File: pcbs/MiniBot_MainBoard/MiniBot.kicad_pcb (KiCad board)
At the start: 4 copper layers, 21.2 x 28 mm, 60 parts, among them IC1 MMC5633NJL, IC2 MIC23050-SYML-TR, J1 Conn_01x08, J2 Conn_01x02, J3 GSB1C41110SSHR, J4 Conn_01x01, U1 ESP32-C3-MINI-1-H4X, U3 MCP73832-2-OT, U4 STSPIN220, U5 STSPIN220

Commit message: led updates
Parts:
- removed D1, D2: LED, Diode_SMD:D_0402_1005Metric
- removed J4: Conn_01x01, TestPoint:TestPoint_Pad_D1.0mm
- removed R17: 5.1k, Resistor_SMD:R_0402_1005Metric
- added LED1: EASV2010RWA0, SamacSys_Parts:EASV2010RWA0, B.Cu at (121.3, 85.4)
- added R4: 10k, Resistor_SMD:R_0402_1005Metric, B.Cu at (127.2, 90.4)
- R8: value 15k -> 12.4k
- moved JP1 1.63 mm to (121.6, 87.9)
- moved IC1 0.66 mm to (128.6, 107.6)
- moved R13 0.61 mm to (124.9, 88.1), turned to 90 degrees
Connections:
- R13 pad 1: Net-(D2-K) -> /LED_R
- U1 pad 12: /GPIO0 -> /LED_W
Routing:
- net +3V3: track 37.1 -> 57.3 mm, vias 12 -> 13
- net /LED_W: track 0.00 -> 20.1 mm, vias 0 -> 2
- net Net-(LED1-T1-): track 0.00 -> 9.23 mm
- net /GPIO0: track 7.22 -> 0.00 mm, vias 2 -> 0
- net /LED_R: track 0.00 -> 6.80 mm
- net GND: track 94.3 -> 97.6 mm, vias 24 -> 23
- net Net-(D2-K): track 2.47 -> 0.00 mm, vias 1 -> 0
- net Net-(D1-A): track 0.99 -> 0.00 mm
- net /MODE2: track 29.2 -> 28.4 mm
- net +BATT: track 25.8 -> 26.2 mm, vias 0 -> 1
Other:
- board text removed: "3v3"
- board text removed: "CHG"
- board text removed: "M1"
- board text removed: "M2"

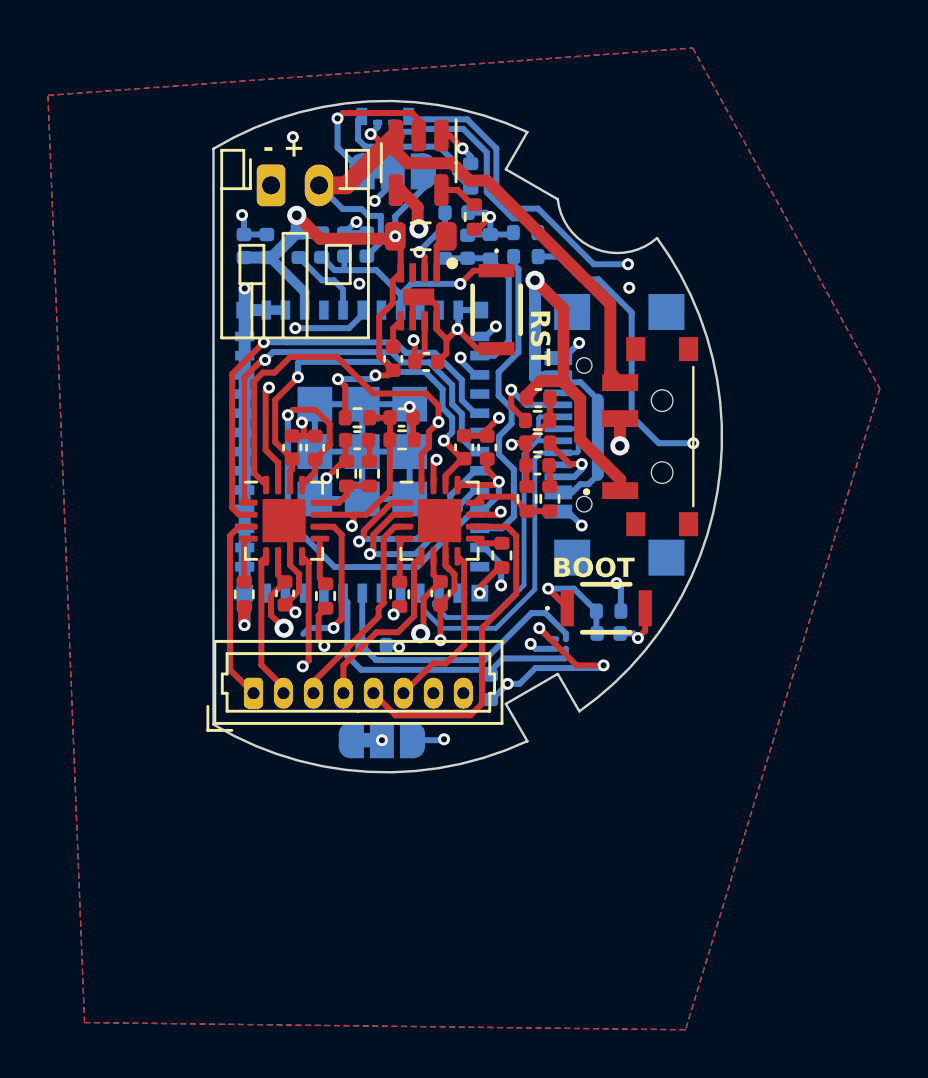
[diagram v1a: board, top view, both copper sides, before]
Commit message: improved pcb thermals
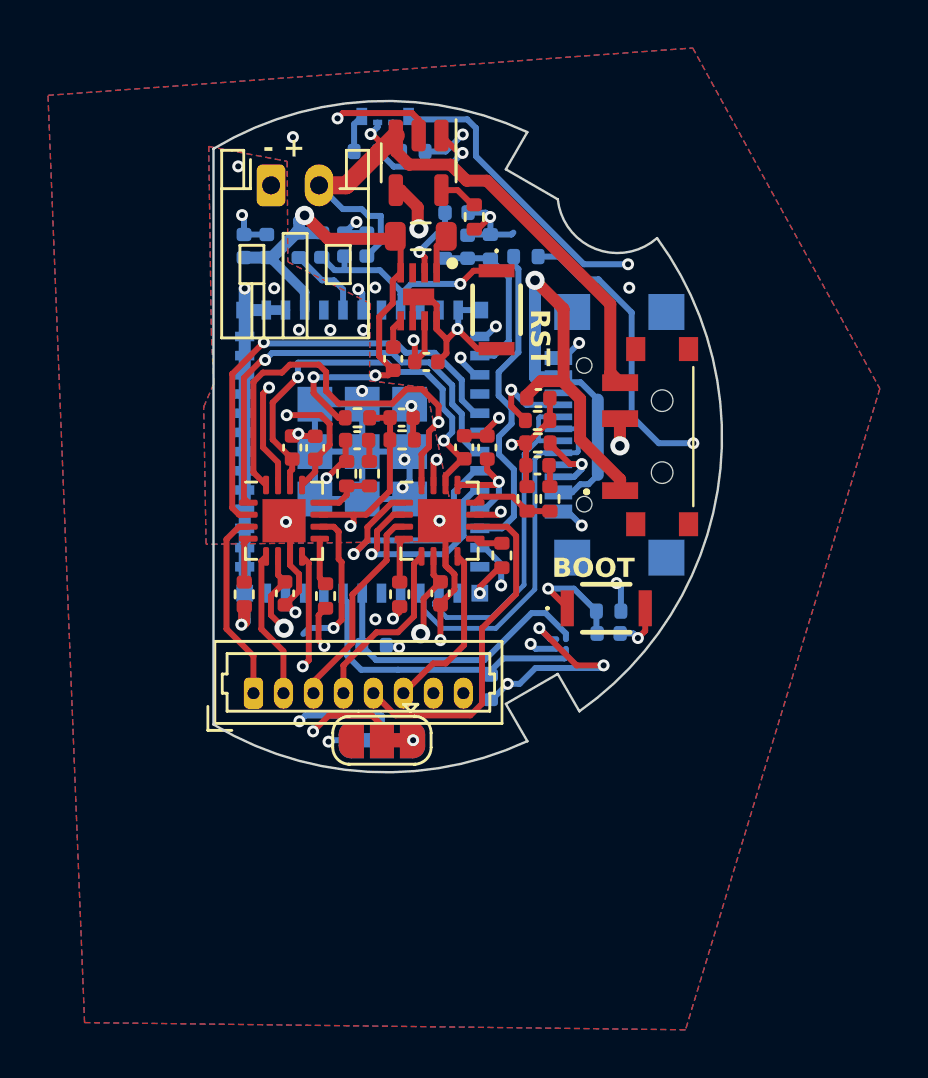
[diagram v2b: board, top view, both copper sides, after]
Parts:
- JP1: moved to F.Cu
- moved JP1 23.7 mm to (121.2, 111.6), turned to 180 degrees
- moved R4 5.79 mm to (122.5, 87.0), turned to 0 degrees
- moved R13 4.47 mm to (120.5, 87.0), turned to 0 degrees
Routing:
- net /MODE2: track 28.4 -> 38.9 mm
- net Net-(LED1-T1-): track 9.23 -> 1.35 mm
- net /LED_R: track 6.80 -> 1.59 mm
- net /MODE1: track 41.9 -> 46.5 mm
- net /M_EN: track 23.8 -> 20.0 mm
- net Net-(U3-STAT): track 1.88 -> 5.18 mm
- net /M_RST: track 22.7 -> 24.9 mm
- net /M1_DIR: track 9.18 -> 11.0 mm
- net GND: track 97.6 -> 96.0 mm, vias 23 -> 34
- net +3V3: track 57.3 -> 56.6 mm, vias 13 -> 14
- net /M1_STEP: track 8.27 -> 8.91 mm
- added copper zone on B.Cu, net GND
- added copper zone on F.Cu, net GND

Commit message: cleanup minibot schematic
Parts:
- moved R13 0.18 mm to (120.5, 87.2)
- moved R4 0.18 mm to (122.4, 87.2)
- moved LED1 0.16 mm to (121.3, 85.5)
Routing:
- net /M0_B1: track 13.0 -> 11.6 mm
- net GND: track 96.0 -> 94.9 mm, vias 34 -> 33
- net /M_RST: track 24.9 -> 25.7 mm
- net /M0_DIR: track 18.3 -> 18.9 mm
- net /M0_STEP: track 19.0 -> 19.5 mm
- net Net-(U3-STAT): track 5.18 -> 5.69 mm
- net +3V3: vias 14 -> 13
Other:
- board text added: "M1"
- board text added: "M2"

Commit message: checkpoint
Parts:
- moved R1 0.98 mm to (126.2, 108.5)
- moved R5 0.65 mm to (126.7, 91.0), turned to -90 degrees
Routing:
- net +3V3: track 56.6 -> 57.6 mm
- net /MODE1: track 46.5 -> 45.5 mm
- net /M_RST: track 25.7 -> 25.2 mm

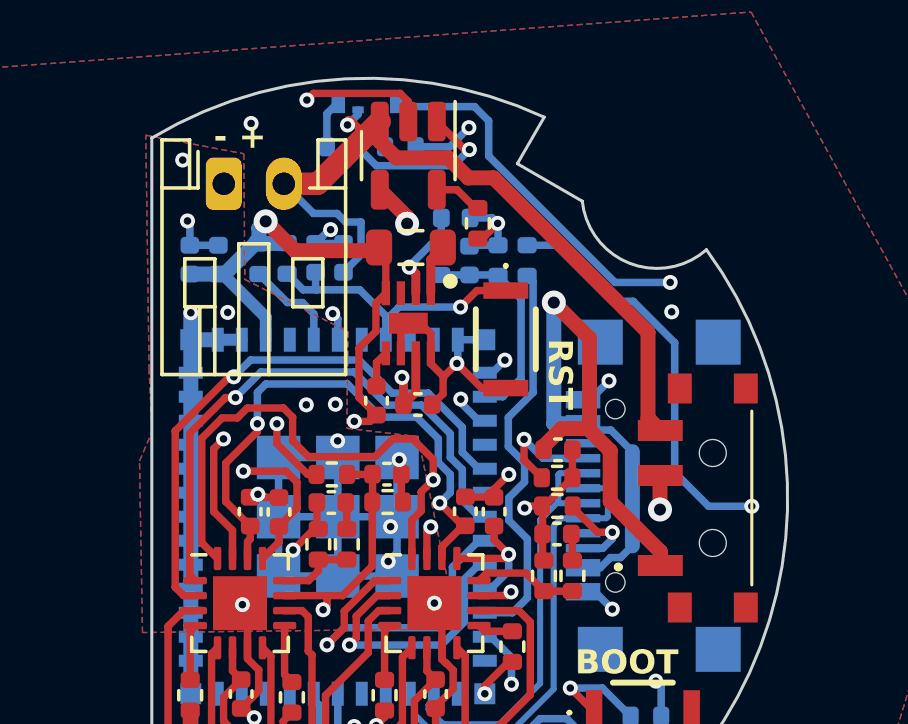
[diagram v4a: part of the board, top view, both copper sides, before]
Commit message: moving imported parts from my global dir to within this repo
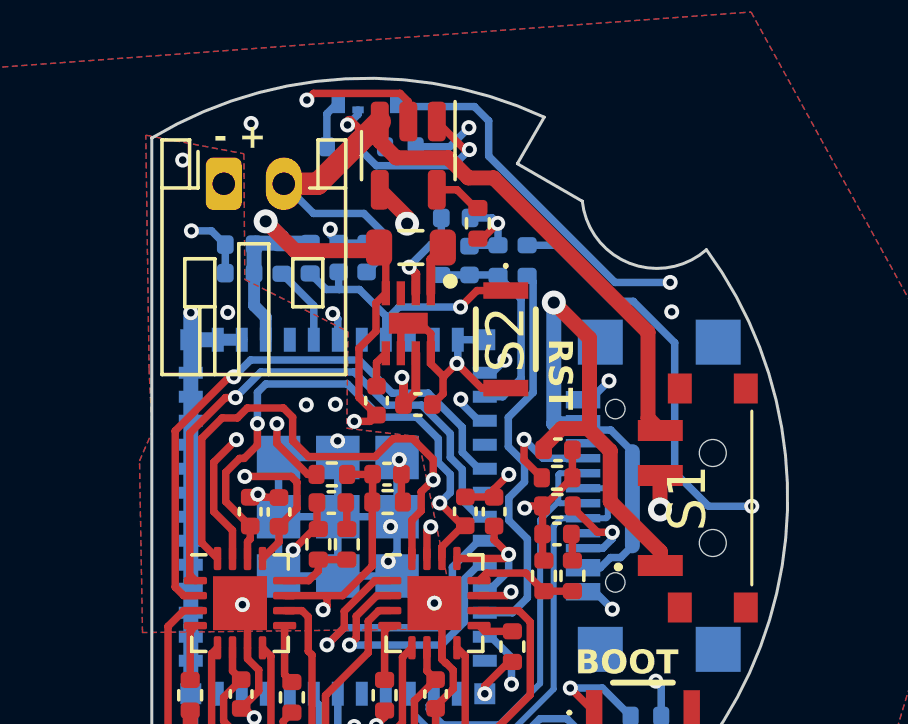
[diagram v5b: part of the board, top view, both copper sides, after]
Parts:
- IC1: footprint SamacSys_Parts:BGA4C40P2X2_85X85X60 -> minibot:BGA4C40P2X2_85X85X60
- J3: footprint SamacSys_Parts:GSB1C41110SSHR -> minibot:GSB1C41110SSHR
- LED1: footprint SamacSys_Parts:EASV2010RWA0 -> minibot:EASV2010RWA0
- S1: footprint SamacSys_Parts:PCM12SMTR -> minibot:PCM12SMTR
- S2, S3: footprint SamacSys_Parts:EVPAWBD4A -> minibot:EVPAWBD4A
- U1: footprint SamacSys_Parts:ESP32C3MINI1H4X -> minibot:ESP32C3MINI1H4X
- moved C2 1.72 mm to (117.1, 91.4), turned to 180 degrees
- moved C1 0.87 mm to (117.1, 90.5), turned to 0 degrees
- moved R3 0.77 mm to (119.4, 90.9)
- moved C10 0.77 mm to (121.3, 90.9)
- moved C3 0.77 mm to (120.4, 90.9)
- moved R6 0.77 mm to (118.5, 90.9)
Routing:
- net +3V3: track 57.6 -> 56.3 mm
- net /RST: track 9.67 -> 8.90 mm
- net /GPIO2: track 3.24 -> 2.64 mm
- net +BATT: track 26.2 -> 26.8 mm

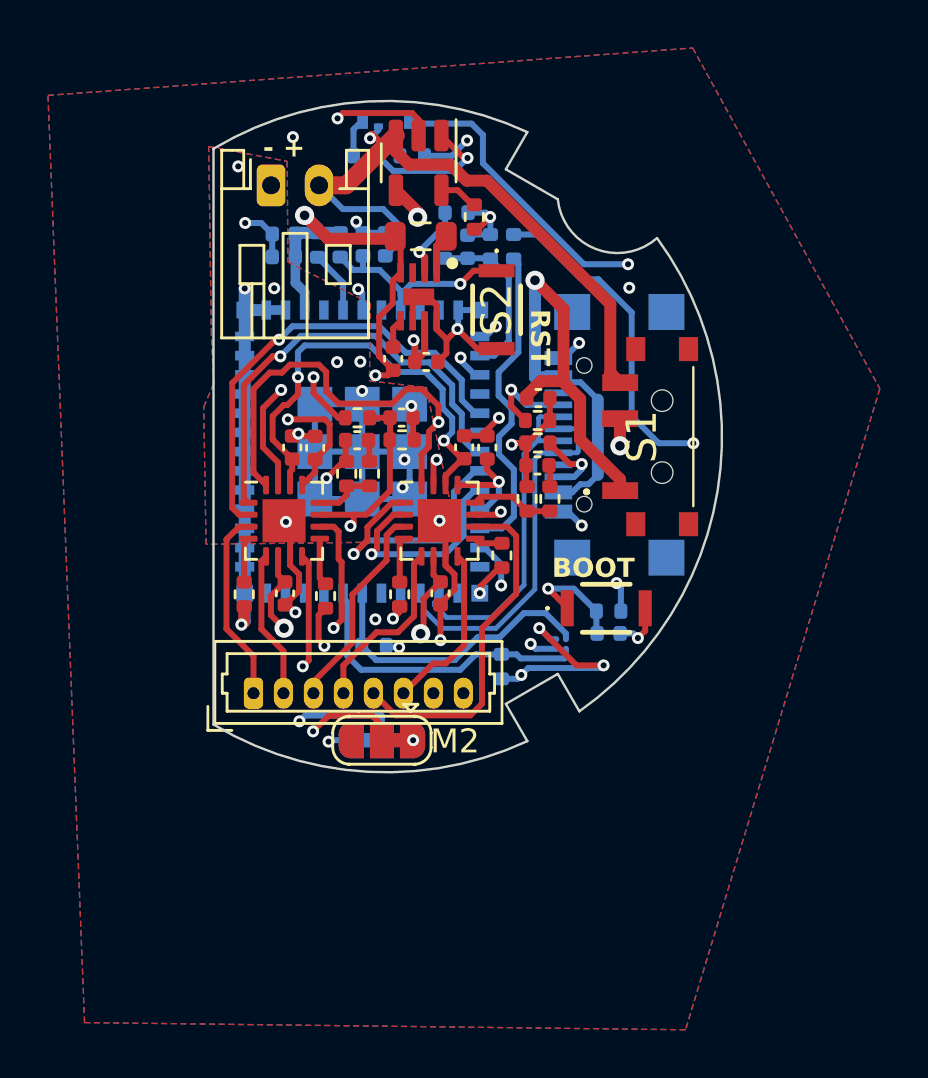
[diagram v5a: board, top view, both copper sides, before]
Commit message: mostly finished server pcb, added pogo charge pins to bots, started charge case pcb
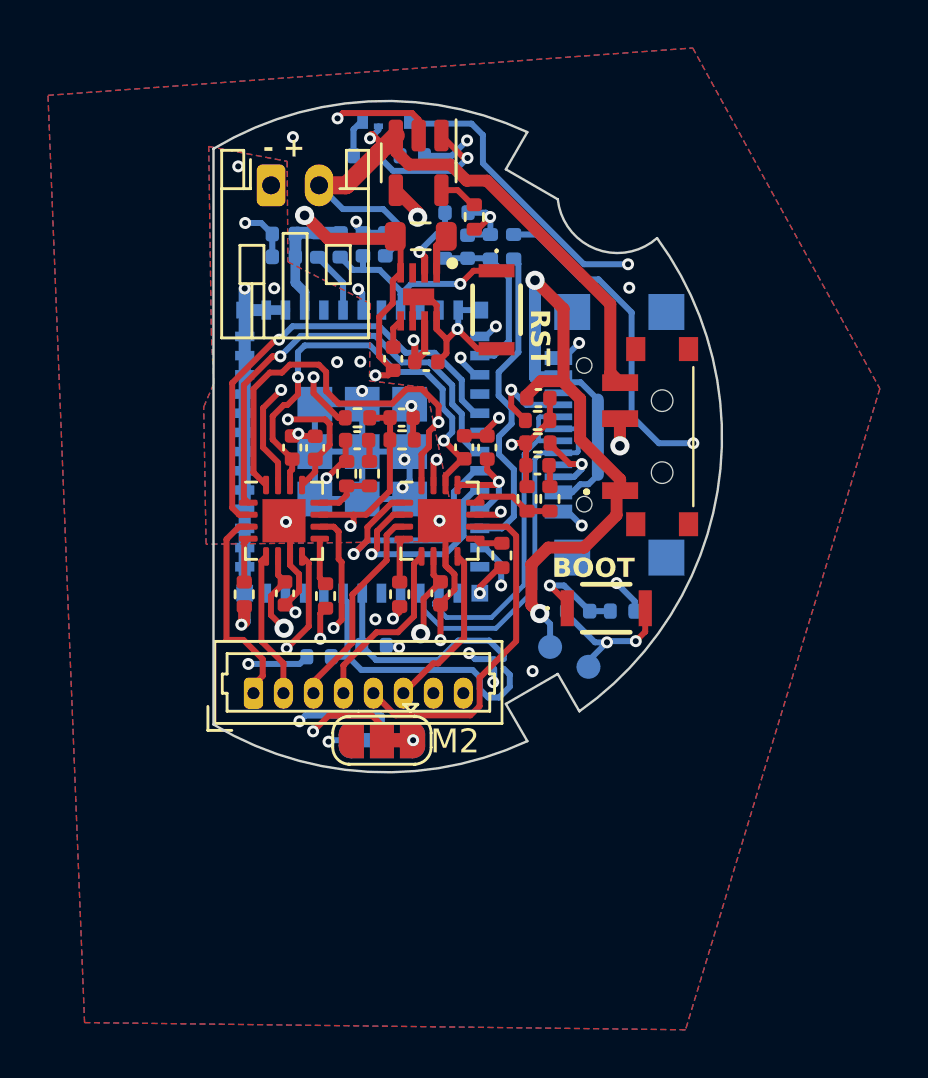
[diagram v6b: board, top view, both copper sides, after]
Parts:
- added TP1: TestPoint, TestPoint:TestPoint_Pad_D1.0mm, B.Cu at (129.8, 108.5)
- added TP2: TestPoint, TestPoint:TestPoint_Pad_D1.0mm, B.Cu at (128.2, 107.7)
- moved R1 7.61 mm to (118.5, 108.1), turned to 0 degrees
- moved IC1 2.72 mm to (126.0, 108.4)
- moved C5 1.57 mm to (129.3, 106.2), turned to 180 degrees
- moved R9 0.58 mm to (131.2, 106.2)
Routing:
- net +5V: track 31.8 -> 41.0 mm, vias 2 -> 3
- net GND: track 95.4 -> 98.6 mm, vias 33 -> 34
- net /SDA: track 12.1 -> 8.91 mm
- net +3V3: track 56.3 -> 54.0 mm
- net /M0_A1: track 8.01 -> 8.75 mm
- net /SCL: track 12.5 -> 12.0 mm
- net /M0_B2: track 10.7 -> 11.2 mm

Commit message: gitignore and pcb updates
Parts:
- moved JP1 0.12 mm to (121.2, 111.7)
- moved JP2 0.12 mm to (121.2, 111.7)
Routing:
- net +3V3: track 54.0 -> 54.9 mm
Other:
- board text added: "+"
- board text added: "-"
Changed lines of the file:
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@@
   )
   (footprint "Jumper:SolderJumper-3_P1.3mm_Bridged12_RoundedPad1.0x1.5mm" (layer "F.Cu")
-    (at 121.17 111.58 180)
+    (at 121.17 111.7 180)
     (descr "SMD Solder 3-pad Jumper, 1x1.5mm rounded Pads, 0.3mm gap, pads 1-2 bridged with 1 copper strip")
     (tags "net tie solder jumper bridged")
@@
   )
   (footprint "Jumper:SolderJumper-3_P1.3mm_Bridged12_RoundedPad1.0x1.5mm" (layer "B.Cu")
-    (at 121.17 111.58)
+    (at 121.17 111.7)
     (descr "SMD Solder 3-pad Jumper, 1x1.5mm rounded Pads, 0.3mm gap, pads 1-2 bridged with 1 copper strip")
     (tags "net tie solder jumper bridged")
@@
   (gr_line (start 121.345 98.94) (end 121.345 112.940014)
     (stroke (width 0.1) (type default)) (layer "F.Fab"))
+  (gr_text "+" (at 127.65 107.75) (layer "B.SilkS")
+    (effects (font (size 0.8 0.8) (thickness 0.15) bold) (justify left bottom mirror))
+  )
+  (gr_text "-" (at 131.55 108.8) (layer "B.SilkS")
+    (effects (font (size 0.8 0.8) (thickness 0.15) bold) (justify left bottom mirror))
+  )
   (gr_text "M1" (at 125.44 112.17) (layer "B.SilkS")
     (effects (font (size 1 1) (thickness 0.15)) (justify left bottom mirror))
@@
   (via (at 124.32 94.44) (size 0.5) (drill 0.25) (layers "F.Cu" "B.Cu") (net 15))
   (via (at 115.45 92.75) (size 0.5) (drill 0.25) (layers "F.Cu" "B.Cu") (net 15))
-  (via (at 122.47 111.58) (size 0.5) (drill 0.25) (layers "F.Cu" "B.Cu") (net 15))
+  (via (at 122.47 111.700002) (size 0.5) (drill 0.25) (layers "F.Cu" "B.Cu") (net 15))
   (via (at 131.749988 107.45) (size 0.5) (drill 0.25) (layers "F.Cu" "B.Cu") (net 15))
   (via (at 118.6 107.35002) (size 0.5) (drill 0.25) (layers "F.Cu" "B.Cu") (net 15))
@@
   (segment (start 121.95 92.1) (end 121.95 90.8) (width 0.25) (layer "F.Cu") (net 19))
   (segment (start 121.62 92.43) (end 121.95 92.1) (width 0.25) (layer "F.Cu") (net 19))
+  (segment (start 119.809319 111.639319) (end 119.87 111.7) (width 0.25) (layer "F.Cu") (net 19))
   (segment (start 121.43 96.37) (end 121.64 96.16) (width 0.25) (layer "F.Cu") (net 19))
   (segment (start 121.055 95.575) (end 121.055 93.935) (width 0.25) (layer "F.Cu") (net 19))
@@
   (segment (start 121.62 93.37) (end 121.62 92.43) (width 0.25) (layer "F.Cu") (net 19))
   (segment (start 118.922223 90.68) (end 121.62 90.68) (width 0.5) (layer "F.Cu") (net 19))
+  (segment (start 118.944971 111.639319) (end 119.809319 111.639319) (width 0.25) (layer "F.Cu") (net 19))
   (segment (start 117.945574 89.703351) (end 118.922223 90.68) (width 0.5) (layer "F.Cu") (net 19))
   (segment (start 118.320003 96.449998) (end 118.320003 97.110003) (width 0.25) (layer "F.Cu") (net 19))
@@
   (segment (start 115.89 107.226116) (end 115.025 108.091116) (width 0.25) (layer "In2.Cu") (net 71))
   (segment (start 115.657708 110.79) (end 117.73 110.79) (width 0.25) (layer "In2.Cu") (net 71))
-  (segment (start 121.14 110.55) (end 117.97 110.55) (width 0.25) (layer "B.Cu") (net 71))
+  (segment (start 121.17 111.7) (end 121.17 110.72) (width 0.25) (layer "B.Cu") (net 71))
+  (segment (start 121.17 110.72) (end 121 110.55) (width 0.25) (layer "B.Cu") (net 71))
+  (segment (start 121 110.55) (end 117.97 110.55) (width 0.25) (layer "B.Cu") (net 71))
   (segment (start 117.97 110.55) (end 117.73 110.79) (width 0.25) (layer "B.Cu") (net 71))
-  (segment (start 121.17 111.58) (end 121.17 110.58) (width 0.25) (layer "B.Cu") (net 71))
-  (segment (start 121.17 110.58) (end 121.14 110.55) (width 0.25) (layer "B.Cu") (net 71))
+  (segment (start 118.3 111.21) (end 118.955 110.555) (width 0.25) (layer "F.Cu") (net 72))
   (segment (start 116.215 97.735) (end 116.97 96.98) (width 0.25) (layer "F.Cu") (net 72))
   (segment (start 116.84 100.9425) (end 116.84 100.004314) (width 0.25) (layer "F.Cu") (net 72))
+  (segment (start 120.76 110.555) (end 121.17 110.965) (width 0.25) (layer "F.Cu") (net 72))
   (segment (start 123.32 100.017193) (end 123.449709 99.887484) (width 0.25) (layer "F.Cu") (net 72))
   (segment (start 116.215 99.379314) (end 116.215 97.735) (width 0.25) (layer "F.Cu") (net 72))
+  (segment (start 121.17 110.965) (end 121.17 111.7) (width 0.25) (layer "F.Cu") (net 72))
   (segment (start 116.84 100.004314) (end 116.215 99.379314) (width 0.25) (layer "F.Cu") (net 72))
-  (segment (start 118.955 110.555) (end 120.76 110.555) (width 0.25) (layer "F.Cu") (net 72))
-  (segment (start 121.17 110.965) (end 121.17 111.58) (width 0.25) (layer "F.Cu") (net 72))
   (segment (start 123.32 100.94125) (end 123.32 100.017193) (width 0.25) (layer "F.Cu") (net 72))
-  (segment (start 120.76 110.555) (end 121.17 110.965) (width 0.25) (layer "F.Cu") (net 72))
-  (segment (start 118.3 111.21) (end 118.955 110.555) (width 0.25) (layer "F.Cu") (net 72))
+  (segment (start 118.955 110.555) (end 120.76 110.555) (width 0.25) (layer "F.Cu") (net 72))
   (via (at 123.449709 99.887484) (size 0.5) (drill 0.25) (layers "F.Cu" "B.Cu") (net 72))
   (via (at 118.3 111.21) (size 0.5) (drill 0.25) (layers "F.Cu" "B.Cu") (net 72))
